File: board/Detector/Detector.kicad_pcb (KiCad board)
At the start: 2 copper layers, 29.5 x 100 mm, 62 parts, among them J1 Conn_02x04_Odd_Even, J2 Conn_02x04_Odd_Even, J3 Conn_01x03, Q1 Q_Photo_NPN, Q2 Q_Photo_NPN, Q3 Q_Photo_NPN, Q4 Q_Photo_NPN, Q5 Q_Photo_NPN, Q6 Q_Photo_NPN, Q7 Q_Photo_NPN, Q8 Q_Photo_NPN, U1 LM339, U2 LM339, U3 LP2950-3.3_TO92

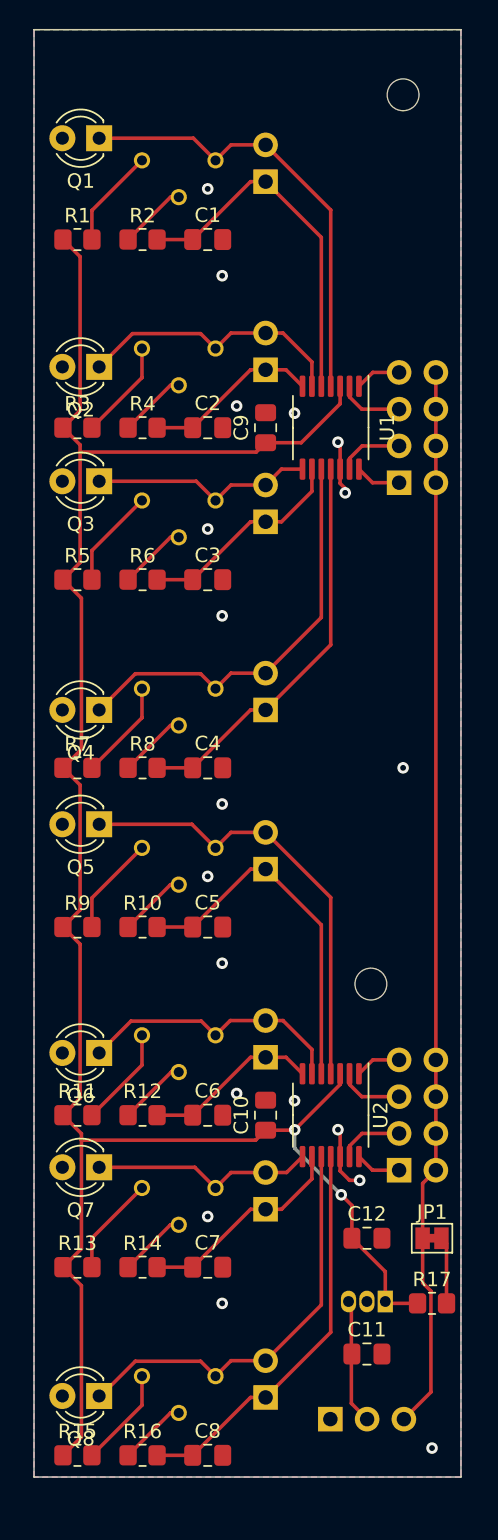
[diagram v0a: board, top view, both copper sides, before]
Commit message: Complete layout with top pour
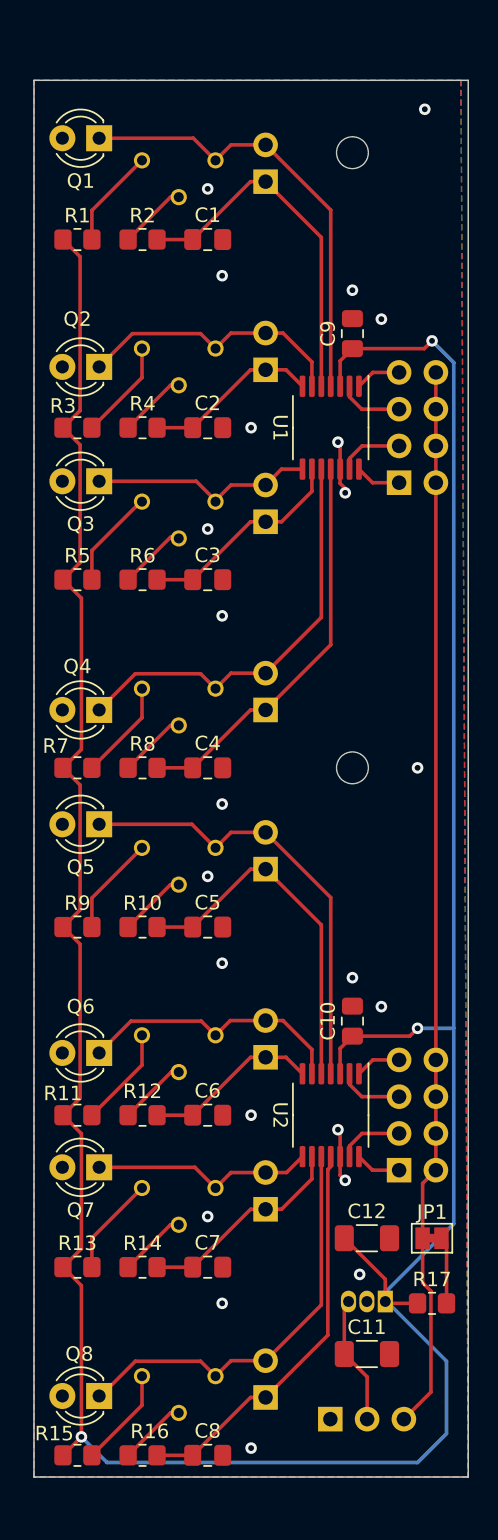
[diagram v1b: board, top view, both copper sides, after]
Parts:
- C11, C12: footprint Capacitor_SMD:C_0805_2012Metric_Pad1.18x1.45mm_HandSolder -> Capacitor_SMD:C_1206_3216Metric_Pad1.33x1.80mm_HandSolder
- moved REF** 15.0 mm to (132.7, 97.1)
- moved C10 8.85 mm to (132.7, 114.6)
- moved C9 8.85 mm to (132.7, 67.1)
- moved REF** 5.32 mm to (132.7, 54.6)
- moved RV3 0.08 mm to (120.7, 75.1)
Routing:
- net +3V3: track 148.6 -> 224.5 mm, vias 2 -> 3
- net GND: track 8.57 -> 7.41 mm, vias 19 -> 23
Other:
- board size 29.5 x 100 mm -> 30 x 96.5 mm
- board text added: "1"
- board text added: "2"
- board text added: "3"
- board text added: "4"
- board text added: "5"
- board text added: "5V"
- board text added: "6"
- board text added: "7"
- board text added: "8"
- board text added: "GND"
- board text added: "OUT"

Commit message: Final version of detector and gerbers
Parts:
- moved C10 8.51 mm to (127.2, 121.1), turned to -90 degrees
- moved C9 8.51 mm to (127.2, 73.6), turned to -90 degrees
- turned C12 to 180 degrees
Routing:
- net +3V3: track 224.5 -> 171.1 mm, vias 3 -> 2
- net GND: track 7.41 -> 36.5 mm, vias 23 -> 12
- removed copper zone on F.Cu, net GND
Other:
- board text added: "Saint Gimp Ballistic Chronograph Detector 1.00"

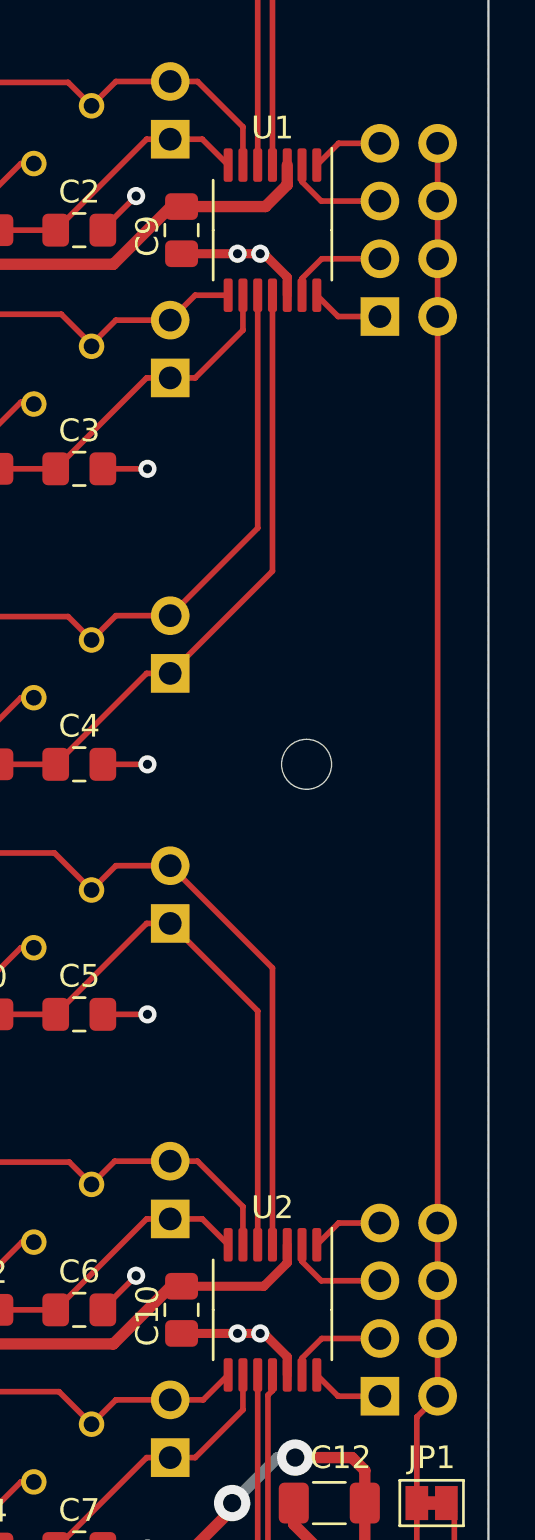
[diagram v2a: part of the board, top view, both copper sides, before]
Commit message: Fix the order of jumper links
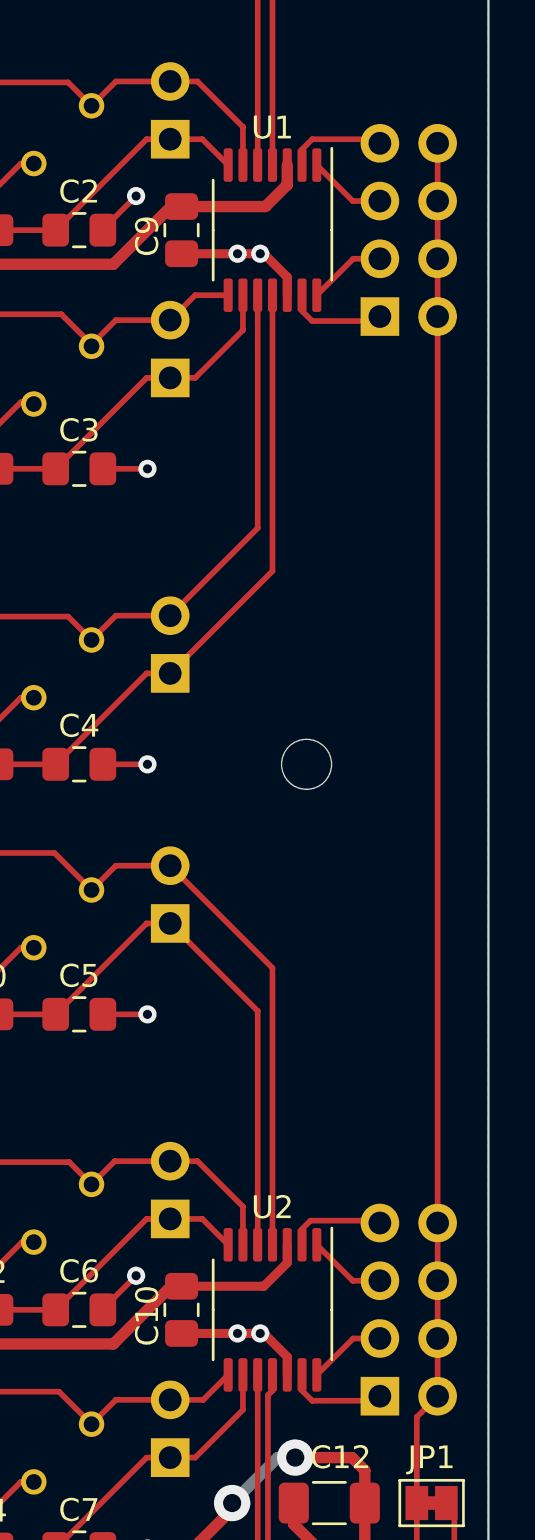
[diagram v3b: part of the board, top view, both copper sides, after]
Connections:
- U1 pad 1: Net-(J1-Pad7) -> Net-(J1-Pad5)
- U1 pad 13: Net-(J1-Pad3) -> Net-(J1-Pad1)
- U1 pad 14: Net-(J1-Pad1) -> Net-(J1-Pad3)
- U1 pad 2: Net-(J1-Pad5) -> Net-(J1-Pad7)
- U2 pad 1: Net-(J2-Pad7) -> Net-(J2-Pad5)
- U2 pad 13: Net-(J2-Pad3) -> Net-(J2-Pad1)
- U2 pad 14: Net-(J2-Pad1) -> Net-(J2-Pad3)
- U2 pad 2: Net-(J2-Pad5) -> Net-(J2-Pad7)
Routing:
- net Net-(J2-Pad1): track 3.16 -> 4.38 mm
- net Net-(J1-Pad1): track 3.16 -> 4.38 mm
- net Net-(J1-Pad7): track 3.17 -> 4.38 mm
- net Net-(J2-Pad7): track 3.17 -> 4.31 mm
- net Net-(J2-Pad5): track 4.51 -> 3.43 mm
- net Net-(J2-Pad3): track 4.52 -> 3.44 mm
- net Net-(J1-Pad5): track 4.51 -> 3.43 mm
- net Net-(J1-Pad3): track 4.52 -> 3.44 mm

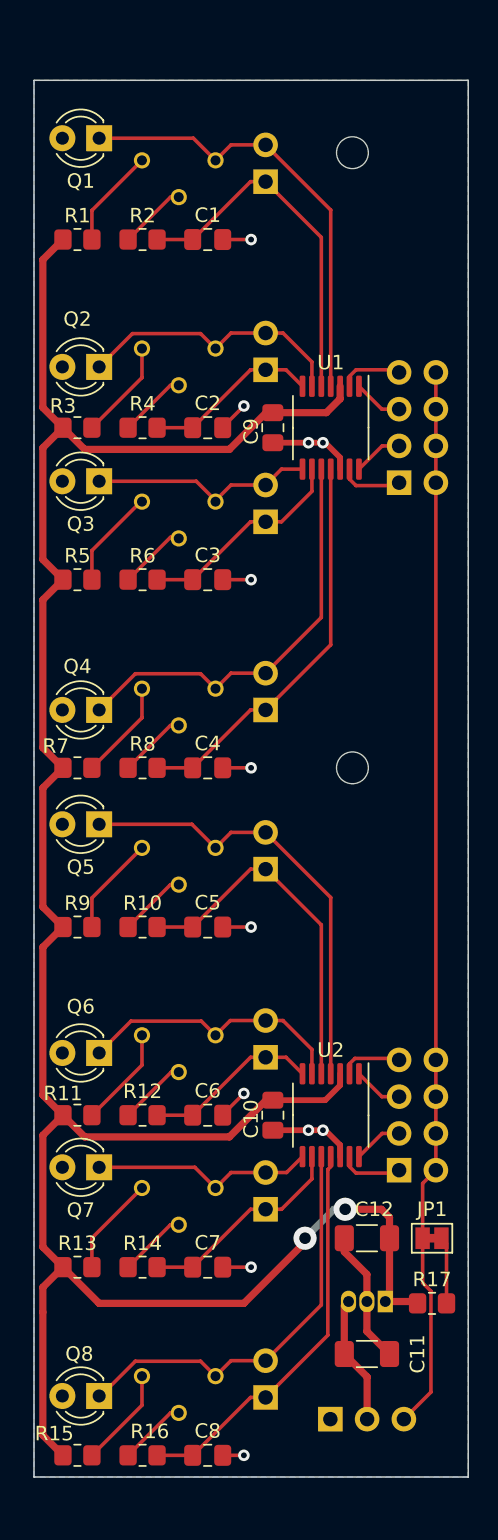
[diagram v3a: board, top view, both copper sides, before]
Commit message: Increase led and phototransistor spacing to better handle angled holes
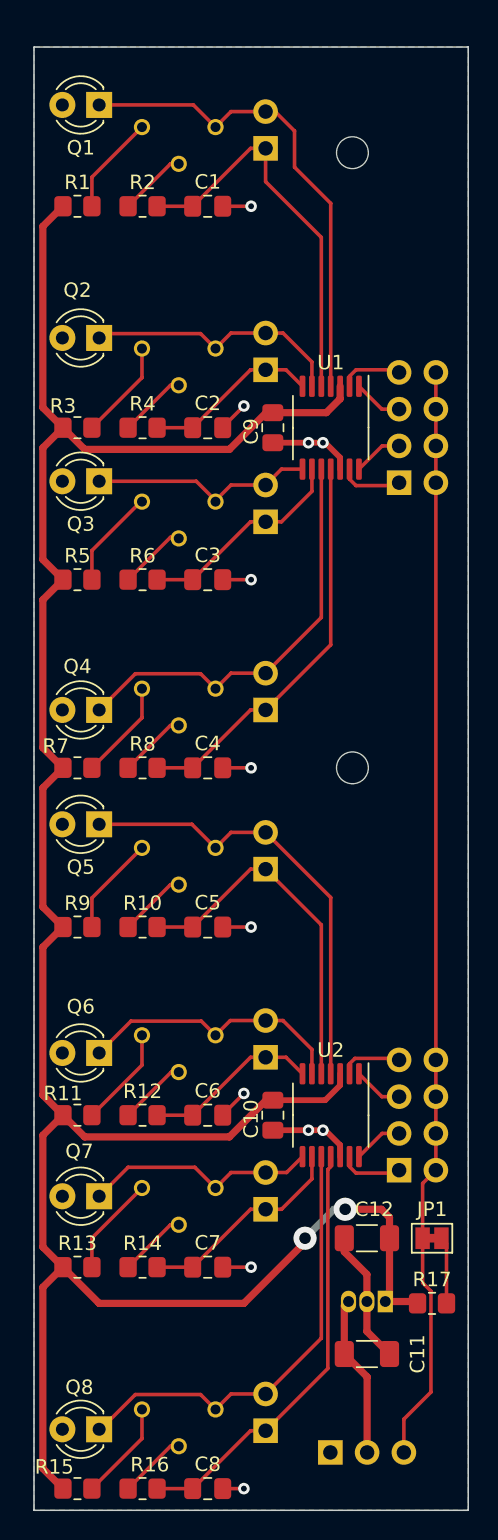
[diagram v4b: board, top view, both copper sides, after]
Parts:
- moved C8 2.30 mm to (122.7, 146.9)
- moved J3 2.30 mm to (131.2, 144.4)
- moved R15 2.30 mm to (113.7, 146.9)
- moved R16 2.30 mm to (118.2, 146.9)
- moved RV8 2.30 mm to (120.7, 137.9)
- moved TP8 2.30 mm to (126.7, 142.9)
- moved C1 2.30 mm to (122.7, 58.3)
- moved Q1 2.30 mm to (115.2, 51.3)
- moved R1 2.30 mm to (113.7, 58.3)
- moved R2 2.30 mm to (118.2, 58.3)
- moved RV1 2.30 mm to (120.7, 49.3)
- moved TP1 2.30 mm to (126.7, 54.3)
- moved Q8 2.30 mm to (115.2, 142.8)
- moved Q2 2.00 mm to (115.2, 67.4)
- moved Q7 2.00 mm to (115.2, 126.7)
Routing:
- net +3V3: track 171.1 -> 175.7 mm
- net Net-(Q1-Pad1): track 31.1 -> 33.8 mm
- net Net-(C8-Pad1): track 27.7 -> 30.0 mm
- net /Group-A/Group-A-Output: track 73.7 -> 76.0 mm
- net +5V: track 8.90 -> 11.2 mm
- net Net-(C1-Pad1): track 24.9 -> 27.2 mm
- net Net-(Q8-Pad1): track 29.1 -> 31.4 mm
- net Net-(Q7-Pad1): track 15.5 -> 16.4 mm
- net Net-(Q2-Pad1): track 19.0 -> 18.2 mm
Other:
- board size 30 x 96.5 mm -> 30 x 101.1 mm
- board text added: "Saint Gimp Ballistic Chronograph Detector 1.10"
- board text removed: "Saint Gimp Ballistic Chronograph Detector 1.00"

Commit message: Detector changes to better control overall bias level
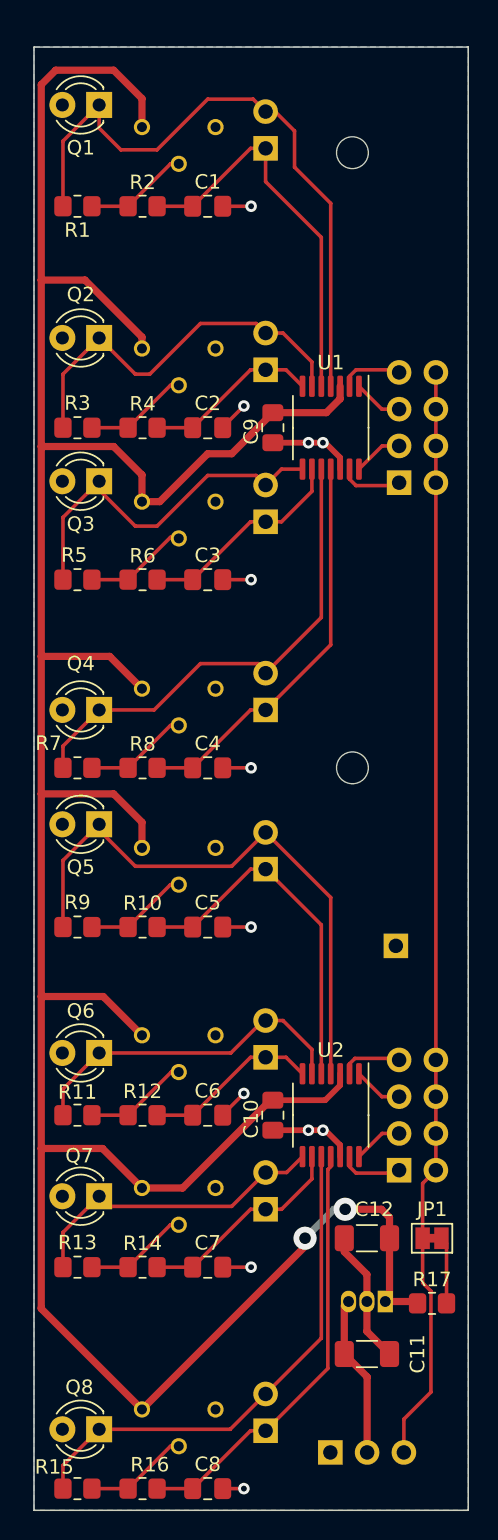
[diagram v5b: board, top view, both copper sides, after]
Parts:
- added TP9: TestPoint, Connector_PinHeader_2.54mm:PinHeader_1x01_P2.54mm_Vertical, B.Cu at (135.7, 109.4)
- Q1, Q2, Q3, Q4, Q5, Q6, Q7, Q8: value Q_Photo_NPN -> SFH 314 FA-2/3; footprint LED_THT:LED_D3.0mm_Clear -> LED_THT:LED_D3.0mm_IRBlack
- R1, R11, R13, R15, R3, R5, R7, R9: value 330 -> 1
- RV1, RV2, RV3, RV4, RV5, RV6, RV7, RV8: value 200 -> 5K
- turned R1 to 180 degrees
- turned R11 to 180 degrees
- turned R13 to 180 degrees
- turned R15 to 180 degrees
- turned R3 to 180 degrees
- turned R5 to 180 degrees
- turned R7 to 180 degrees
- turned R9 to 180 degrees
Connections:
- R1 pad 1: +3V3 -> Net-(R1-Pad1)
- R1 pad 2: Net-(R1-Pad2) -> Net-(Q1-Pad1)
- R11 pad 1: +3V3 -> Net-(R11-Pad1)
- R11 pad 2: Net-(R11-Pad2) -> Net-(Q6-Pad1)
- R12 pad 1: Net-(R12-Pad1) -> Net-(R11-Pad1)
- R13 pad 1: +3V3 -> Net-(R14-Pad1)
- R13 pad 2: Net-(R13-Pad2) -> Net-(Q7-Pad1)
- R15 pad 1: +3V3 -> Net-(R15-Pad1)
- R15 pad 2: Net-(R15-Pad2) -> Net-(Q8-Pad1)
- R16 pad 1: Net-(R16-Pad1) -> Net-(R15-Pad1)
- R2 pad 1: Net-(R2-Pad1) -> Net-(R1-Pad1)
- R3 pad 1: +3V3 -> Net-(R4-Pad1)
- R3 pad 2: Net-(R3-Pad2) -> Net-(Q2-Pad1)
- R5 pad 1: +3V3 -> Net-(R5-Pad1)
- R5 pad 2: Net-(R5-Pad2) -> Net-(Q3-Pad1)
- R6 pad 1: Net-(R6-Pad1) -> Net-(R5-Pad1)
- R7 pad 1: +3V3 -> Net-(R8-Pad1)
- R7 pad 2: Net-(R7-Pad2) -> Net-(Q4-Pad1)
- R9 pad 1: +3V3 -> Net-(R10-Pad1)
- R9 pad 2: Net-(R9-Pad2) -> Net-(Q5-Pad1)
- RV1 pad 1: Net-(R1-Pad2) -> +3V3
- RV1 pad 2: Net-(R2-Pad1) -> Net-(R1-Pad1)
- RV1 pad 3: Net-(Q1-Pad1) -> (no net)
- RV2 pad 1: Net-(R3-Pad2) -> +3V3
- RV2 pad 3: Net-(Q2-Pad1) -> (no net)
- RV3 pad 1: Net-(R5-Pad2) -> +3V3
- RV3 pad 2: Net-(R6-Pad1) -> Net-(R5-Pad1)
- RV3 pad 3: Net-(Q3-Pad1) -> (no net)
- RV4 pad 1: Net-(R7-Pad2) -> +3V3
- RV4 pad 3: Net-(Q4-Pad1) -> (no net)
- RV5 pad 1: Net-(R9-Pad2) -> +3V3
- RV5 pad 3: Net-(Q5-Pad1) -> (no net)
- RV6 pad 1: Net-(R11-Pad2) -> +3V3
- RV6 pad 2: Net-(R12-Pad1) -> Net-(R11-Pad1)
- RV6 pad 3: Net-(Q6-Pad1) -> (no net)
- RV7 pad 1: Net-(R13-Pad2) -> +3V3
- RV7 pad 3: Net-(Q7-Pad1) -> (no net)
- RV8 pad 1: Net-(R15-Pad2) -> +3V3
- RV8 pad 2: Net-(R16-Pad1) -> Net-(R15-Pad1)
- RV8 pad 3: Net-(Q8-Pad1) -> (no net)
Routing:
- net +3V3: track 175.7 -> 223.7 mm
- net Net-(Q1-Pad1): track 33.8 -> 44.8 mm
- net Net-(Q3-Pad1): track 15.5 -> 25.7 mm
- net Net-(Q5-Pad1): track 31.2 -> 40.6 mm
- net Net-(Q2-Pad1): track 18.2 -> 27.2 mm
- net Net-(R11-Pad1): track 0.00 -> 7.23 mm
- net Net-(R5-Pad1): track 0.00 -> 7.21 mm
- net Net-(R15-Pad1): track 0.00 -> 7.21 mm
- net Net-(R1-Pad1): track 0.00 -> 7.21 mm
- net Net-(R11-Pad2): track 6.95 -> 0.00 mm
- net Net-(R15-Pad2): track 6.90 -> 0.00 mm
- net Net-(R9-Pad2): track 6.90 -> 0.00 mm
- net Net-(R5-Pad2): track 6.90 -> 0.00 mm
- net Net-(R1-Pad2): track 6.90 -> 0.00 mm
- net Net-(R7-Pad2): track 6.90 -> 0.00 mm
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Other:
- board text added: "Saint Gimp Ballistic Chronograph Detector 1.2.0"
- board text removed: "Saint Gimp Ballistic Chronograph Detector 1.10"

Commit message: Changed connectors, 3D models, added test points
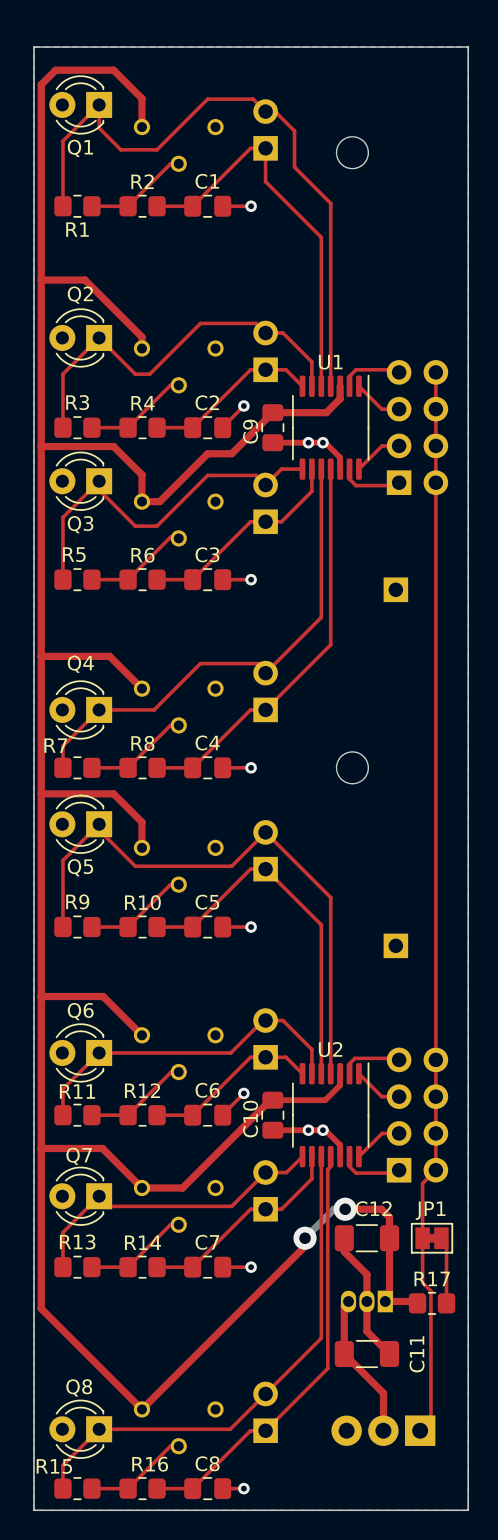
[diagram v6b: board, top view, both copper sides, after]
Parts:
- added TP10: TestPoint, Connector_PinHeader_2.54mm:PinHeader_1x01_P2.54mm_Vertical, B.Cu at (135.7, 84.8)
- J3: footprint SaintGimp:KF2510_Header_1x03_Vertical -> TerminalBlock_TE-Connectivity:TerminalBlock_TE_282834-3_1x03_P2.54mm_Horizontal
- RV1, RV2, RV3, RV4, RV5, RV6, RV7, RV8: value 5K -> 3K
- moved J3 6.38 mm to (137.4, 142.9), turned to 180 degrees
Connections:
- J3 pad 1: GND -> /Group-A/Group-A-Output
- J3 pad 3: /Group-A/Group-A-Output -> GND
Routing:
- net /Group-A/Group-A-Output: track 76.0 -> 74.0 mm
- net +5V: track 11.2 -> 10.2 mm
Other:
- board text added: "Saint Gimp Ballistic Chronograph Detector 1.1.0"
- board text removed: "Saint Gimp Ballistic Chronograph Detector 1.2.0"
